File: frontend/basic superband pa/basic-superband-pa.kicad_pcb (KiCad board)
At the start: 2 copper layers, 64.5 x 60 mm, 68 parts, among them CN1 EDGE, K1 D3002, K2 D3002, P1 BNC, P2 CONN_02X01, Q3 RD16HHF1, T1 TRANSFO, T2 8:1, T3 4:1, T4 OUT_TRANSF, U1 LP2951-50D, U2 LVT827

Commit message: Second pass of superband
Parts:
- added D1: YEL LED (Band1), LEDs:LED-0805, F.Cu at (144.8, 90.1)
- added D2: RED LED (PTT), LEDs:LED-0805, F.Cu at (169.9, 63.3)
- added D3: GRN LED (PWR ON), LEDs:LED-0805, F.Cu at (183.8, 71.2)
- added R13: 4.99k, Resistors_SMD:R_0805_HandSoldering, F.Cu at (189.0, 71.2)
- added R3: 4.99k, Resistors_SMD:R_0805_HandSoldering, F.Cu at (160.0, 89.9)
- added R9: 4.99k, Resistors_SMD:R_0805_HandSoldering, B.Cu at (176.6, 52.6)
- moved C30 3.01 mm to (188.7, 63.6), turned to 0 degrees
- moved R8 1.10 mm to (188.4, 55.3)
- moved MountingHole_4mm 0.22 mm to (189.7, 39.5)
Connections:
- net Net-(K1-Pad10) renamed BAND1
- CN1 pad B12: USEROUT0 -> Net-(CN1-PadB12)
- CN1 pad B16: Net-(CN1-PadB16) -> USEROUT4
- U2 pad 3: USEROUT0 -> USEROUT4
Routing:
- net USEROUT0: track 28.7 -> 0.00 mm, vias 2 -> 0
- net USEROUT4: track 0.00 -> 26.3 mm, vias 0 -> 2
- net Net-(C17-Pad1): track 135.6 -> 161.3 mm, vias 5 -> 6
- net Net-(D1-Pad2): track 0.00 -> 15.2 mm
- net BAND1: track 13.9 -> 28.9 mm, vias 0 -> 2
- net Net-(D2-Pad2): track 0.00 -> 14.4 mm, vias 0 -> 1
- net /PTT: track 52.2 -> 61.8 mm
- net GND: track 90.9 -> 99.3 mm
- net Net-(D3-Pad2): track 0.00 -> 2.80 mm

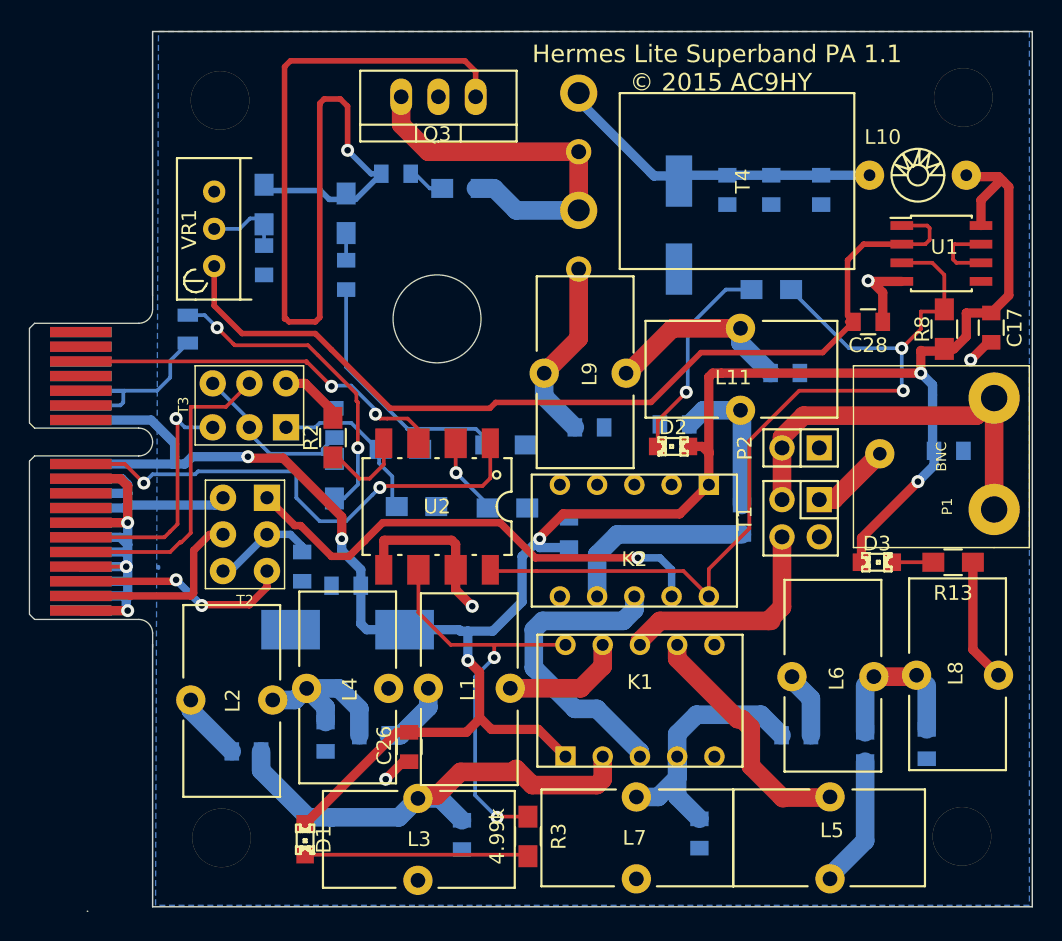
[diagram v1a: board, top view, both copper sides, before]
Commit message: modify mounting holes
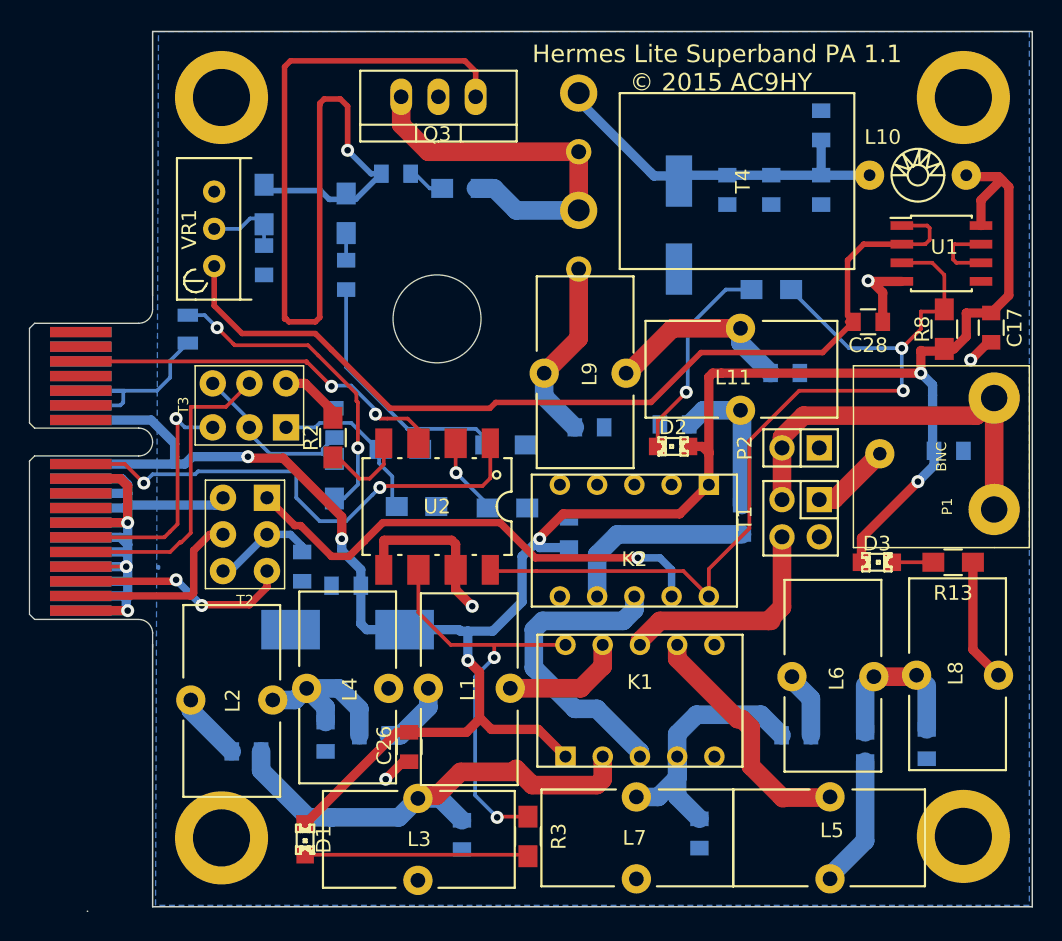
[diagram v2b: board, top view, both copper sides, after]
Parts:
- removed MountingHole_4mm (x4): VAL**, Mounting_Holes:MountingHole_4mm
- added C1: 0.1uF, HERMESLITE:C_0805, B.Cu at (180.0, 41.4)
- added MH: VAL**, HERMESLITE:MH, F.Cu at (189.7, 39.5)
- added MH: VAL**, HERMESLITE:MH, F.Cu at (139.1, 39.5)
- added MH: VAL**, HERMESLITE:MH, F.Cu at (189.7, 89.9)
- added MH: VAL**, HERMESLITE:MH, F.Cu at (139.1, 90.0)
- C12, C15, C16, C19, C26, C28: value 0.01uF -> 0.1uF
- C18: value 120pF -> 150pF
- C23: value 120pF -> 220pF
- C24: value 82pF -> 150pF
- L11, L9: value 192nH -> 240nH
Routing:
- net Net-(C1-Pad2): track 23.0 -> 25.4 mm

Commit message: final 1.2 changes
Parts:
- added P3: Ext PTT, Pin_Headers:Pin_Header_Straight_1x02, F.Cu at (168.7, 52.7)
- added P4: 12-13.8v, Pin_Headers:Pin_Header_Straight_1x02, F.Cu at (184.3, 38.2)
- added R14: 4.99k, Resistors_SMD:R_0805_HandSoldering, B.Cu at (166.6, 68.8)
- C17, C28: value 0.1uF -> 1uF
- R1, R2: value 1.2k -> 270
- moved C22 5.40 mm to (170.2, 42.8), turned to 90 degrees
- moved C19 3.01 mm to (176.8, 48.8)
- moved C20 3.00 mm to (179.9, 48.8)
- moved C21 3.00 mm to (173.6, 48.8)
- moved C4 1.22 mm to (148.6, 72.1)
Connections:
- K2 pad 2: Net-(K2-Pad2) -> GND
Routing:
- net Net-(K2-Pad3): track 0.00 -> 15.2 mm, vias 0 -> 1
- net Net-(C1-Pad2): track 25.4 -> 40.2 mm
- net Net-(C17-Pad1): track 161.3 -> 173.6 mm
- net Net-(K2-Pad9): track 33.4 -> 36.4 mm
- net Net-(K2-Pad4): track 0.00 -> 2.55 mm
- net Net-(D2-Pad2): track 14.4 -> 13.8 mm
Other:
- net class Power: trace_width 0.635 -> 0.78
- net class Power-Wide added: clearance 0.254, trace_width 2.4, via_dia 0.889, via_drill 0.635
- board text added: "+"
- board text added: "Band 1"
- board text added: "Hermes Lite Superband PA 1.2 © 2015 AC9HY"
- board text added: "PTT"
- board text added: "PWR"
- board text removed: "Hermes Lite Superband PA 1.1 © 2015 AC9HY"

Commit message: cleanup, minor superband changes
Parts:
- removed C18, C24: 150pF, HERMESLITE:C_0805
- removed C23: 220pF, HERMESLITE:C_0805
- removed L11, L9: 240nH, Choke_Toroid_ThroughHole:Choke_Toroid_6,5x13mm_Vertical
- removed P2: CONN_02X01, Pin_Headers:Pin_Header_Straight_2x01
- removed T1: TRANSFO, Socket_Strips:Socket_Strip_Straight_2x02
- removed U2: LVT827, Power_Integrations:SMD-8
- added D4: DIODESCH2, HERMESLITE:SOD323, F.Cu at (144.8, 72.0)
- added Q1: FDV301, HERMESLITE:SOT-23-GDS, F.Cu at (158.1, 66.7)
- added Q2: FDV301, HERMESLITE:SOT-23-GDS, F.Cu at (151.5, 64.0)
- added R15: 10k, Resistors_SMD:R_0805_HandSoldering, F.Cu at (156.9, 62.9)
- added R16: 10k, Resistors_SMD:R_0805_HandSoldering, B.Cu at (153.3, 72.2)
- C22: value 10uF 16V -> 10uF 25V
- C7: value 47uF 16V -> 47uF 25V
- R1, R2: value 270 -> 499
- R10, R12: value DNI -> 270
- R11: value 0 -> 18
- moved L10 15.7 mm to (174.3, 54.6)
- moved C20 13.3 mm to (166.7, 49.5), turned to 0 degrees
- moved P3 10.4 mm to (163.9, 62.0), turned to 180 degrees
- moved R9 9.14 mm to (177.4, 61.7)
- moved C1 8.03 mm to (173.6, 46.2), turned to 180 degrees
- moved R1 6.53 mm to (152.4, 69.7), turned to 180 degrees
- moved C19 4.25 mm to (173.6, 51.6), turned to 180 degrees
- moved C21 0.20 mm to (173.6, 49.0), turned to 180 degrees
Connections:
- C29 pad 2: Net-(C24-Pad2) -> Net-(C29-Pad2)
- P1 pad 1: Net-(P1-Pad1) -> Net-(K1-Pad8)
- P1 pad 2: Net-(P1-Pad2) -> GND
- R1 pad 2: GND -> PTT
- R2 pad 2: GND -> USEROUT4
- T4 pad 4: Net-(C18-Pad2) -> Net-(C29-Pad2)
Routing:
- net Net-(P1-Pad2): track 27.4 -> 0.00 mm
- net Net-(C29-Pad2): track 0.00 -> 23.9 mm
- net Net-(C17-Pad1): track 173.6 -> 189.9 mm
- net Net-(C23-Pad2): track 13.2 -> 0.00 mm
- net Net-(C18-Pad2): track 12.6 -> 0.00 mm
- net Net-(C24-Pad2): track 10.7 -> 0.00 mm
- net Net-(C1-Pad2): track 40.2 -> 30.5 mm
- net PTT: track 35.0 -> 25.6 mm, vias 2 -> 1
- net Net-(K1-Pad8): track 15.9 -> 24.5 mm
- net BAND1: track 28.9 -> 36.9 mm, vias 2 -> 4
- net GND: track 99.3 -> 106.6 mm, vias 7 -> 9
- net Net-(K2-Pad3): track 15.2 -> 8.90 mm, vias 1 -> 0
- net USEROUT4: track 26.3 -> 20.8 mm, vias 2 -> 0
- net Net-(P1-Pad1): track 5.43 -> 0.00 mm
- net Net-(Q1-PadG): track 5.32 -> 10.5 mm
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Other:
- board text added: "Hermes Lite Superband PA 1.3 © 2015 AC9HY"
- board text removed: "Hermes Lite Superband PA 1.2 © 2015 AC9HY"
